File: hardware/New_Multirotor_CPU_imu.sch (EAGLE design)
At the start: 85 parts, among them X2 telemetry, X3 programm, X4 sonar

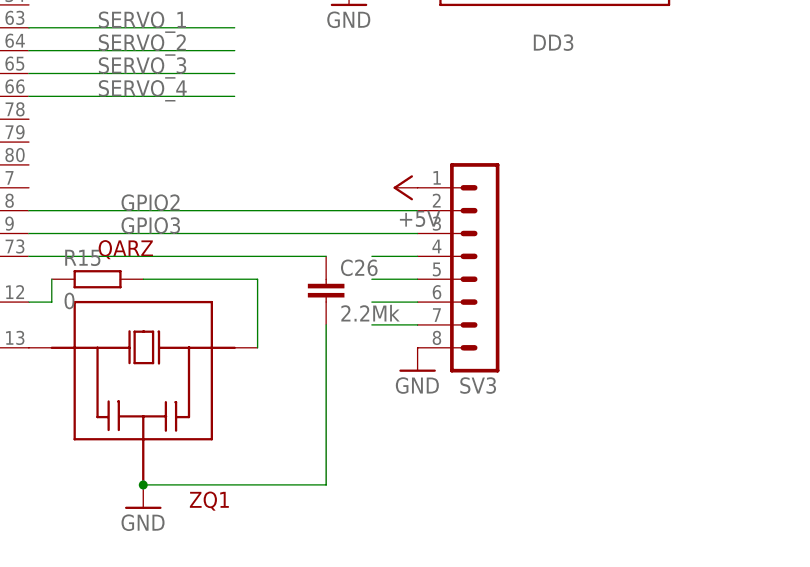
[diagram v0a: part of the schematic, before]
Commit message: Fixes a bug
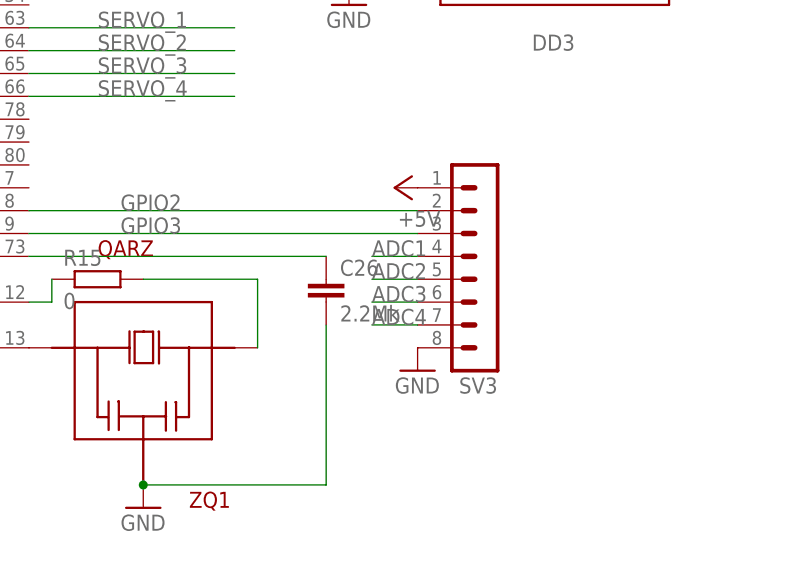
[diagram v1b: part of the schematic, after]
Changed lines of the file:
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@@
 <wire x1="170.18" y1="-12.7" x2="165.1" y2="-12.7" width="0.1524" layer="91"/>
 <pinref part="SV3" gate="1" pin="4"/>
+<label x="165.1" y="-12.7" size="1.778" layer="95"/>
 </segment>
 </net>
@@
 <wire x1="170.18" y1="-20.32" x2="165.1" y2="-20.32" width="0.1524" layer="91"/>
 <pinref part="SV3" gate="1" pin="7"/>
+<label x="165.1" y="-20.32" size="1.778" layer="95"/>
 </segment>
 </net>
@@
 <wire x1="170.18" y1="-15.24" x2="165.1" y2="-15.24" width="0.1524" layer="91"/>
 <pinref part="SV3" gate="1" pin="5"/>
+<label x="165.1" y="-15.24" size="1.778" layer="95"/>
 </segment>
 </net>
@@
 <wire x1="170.18" y1="-17.78" x2="165.1" y2="-17.78" width="0.1524" layer="91"/>
 <pinref part="SV3" gate="1" pin="6"/>
-</segment>
-</net>
+<label x="165.1" y="-17.78" size="1.778" layer="95"/>
+</segment>
+</net>

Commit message: Перезалил
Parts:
- removed R11: 0, resistor:R-EU_R0603
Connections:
- removed net N$15: R11.2, R24.1
- removed net XZ1: DD1.PD12, SV2.8
- removed net XZ2: DD1.PD13, DD6.CS, R10.2, SV2.7
- new net CS_FLASH: DD1.PD13, DD6.CS, R10.2
- net +5V: now also RADIO_IN.8; no longer RADIO_IN.10
- net GND: now also RADIO_IN.10; no longer RADIO_IN.8
- net N$7: now also R24.1; no longer R11.1
- net XZ3: now also SV2.7
- net XZ4: now also SV2.8
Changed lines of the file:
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@@
 <part name="R10" library="resistor" deviceset="R-EU_" device="R0603" value="10k"/>
 <part name="P+22" library="supply1" deviceset="VCC" device=""/>
-<part name="R11" library="resistor" deviceset="R-EU_" device="R0603" value="0"/>
 <part name="R13" library="resistor" deviceset="R-EU_" device="R0603" value="0"/>
 <part name="GND29" library="supply1" deviceset="GND" device=""/>
@@
 <instance part="RN2" gate="C" x="73.66" y="149.86" rot="R180"/>
 <instance part="RN2" gate="D" x="99.06" y="149.86"/>
-<instance part="P+17" gate="1" x="78.74" y="185.42"/>
-<instance part="GND11" gate="1" x="68.58" y="154.94" rot="R270"/>
+<instance part="P+17" gate="1" x="73.66" y="175.26"/>
+<instance part="GND11" gate="1" x="58.42" y="157.48" rot="R270"/>
 <instance part="P+20" gate="VCC" x="220.98" y="25.4" rot="R270"/>
 <instance part="DA2" gate="G$1" x="-139.7" y="-96.52"/>
@@
 <instance part="R10" gate="G$1" x="228.6" y="-27.94" rot="R90"/>
 <instance part="P+22" gate="VCC" x="228.6" y="-35.56" rot="R180"/>
-<instance part="R11" gate="G$1" x="-83.82" y="-88.9"/>
 <instance part="R13" gate="G$1" x="-33.02" y="-93.98"/>
 <instance part="GND29" gate="1" x="-40.64" y="-93.98" rot="R270"/>
@@
 </segment>
 <segment>
-<pinref part="RADIO_IN" gate="G$1" pin="8"/>
-<pinref part="GND11" gate="1" pin="GND"/>
-<wire x1="71.12" y1="154.94" x2="78.74" y2="154.94" width="0.1524" layer="91"/>
-</segment>
-<segment>
 <pinref part="C7" gate="G$1" pin="2"/>
 <pinref part="GND13" gate="1" pin="GND"/>
@@
 <pinref part="GND37" gate="1" pin="GND"/>
 </segment>
+<segment>
+<pinref part="RADIO_IN" gate="G$1" pin="10"/>
+<pinref part="GND11" gate="1" pin="GND"/>
+<wire x1="60.96" y1="157.48" x2="78.74" y2="157.48" width="0.1524" layer="91"/>
+</segment>
 </net>
 <net name="N$41" class="0">
@@
 </segment>
 <segment>
-<pinref part="RADIO_IN" gate="G$1" pin="10"/>
-<pinref part="P+17" gate="1" pin="+5V"/>
-<wire x1="78.74" y1="157.48" x2="78.74" y2="182.88" width="0.1524" layer="91"/>
-</segment>
-<segment>
 <wire x1="236.22" y1="-66.04" x2="228.6" y2="-66.04" width="0.1524" layer="91"/>
 <pinref part="P+7" gate="1" pin="+5V"/>
@@
 <pinref part="SV3" gate="1" pin="1"/>
 <pinref part="P+18" gate="1" pin="+5V"/>
+</segment>
+<segment>
+<pinref part="RADIO_IN" gate="G$1" pin="8"/>
+<wire x1="78.74" y1="154.94" x2="73.66" y2="154.94" width="0.1524" layer="91"/>
+<wire x1="73.66" y1="154.94" x2="73.66" y2="172.72" width="0.1524" layer="91"/>
+<pinref part="P+17" gate="1" pin="+5V"/>
 </segment>
 </net>
@@
 </segment>
 </net>
-<net name="XZ1" class="0">
-<segment>
-<pinref part="DD1" gate="G$1" pin="PD12"/>
-<wire x1="33.02" y1="-15.24" x2="5.08" y2="-15.24" width="0.1524" layer="91"/>
-<label x="5.08" y="-15.24" size="1.778" layer="95"/>
+<net name="CS_FLASH" class="0">
+<segment>
+<pinref part="DD1" gate="G$1" pin="PD13"/>
+<wire x1="33.02" y1="-17.78" x2="5.08" y2="-17.78" width="0.1524" layer="91"/>
+<label x="5.08" y="-17.78" size="1.778" layer="95"/>
+</segment>
+<segment>
+<pinref part="DD6" gate="G$1" pin="CS"/>
+<wire x1="231.14" y1="-22.86" x2="228.6" y2="-22.86" width="0.1524" layer="91"/>
+<label x="220.98" y="-22.86" size="1.778" layer="95"/>
+<pinref part="R10" gate="G$1" pin="2"/>
+<junction x="228.6" y="-22.86"/>
+<wire x1="228.6" y1="-22.86" x2="220.98" y2="-22.86" width="0.1524" layer="91"/>
+</segment>
+</net>
+<net name="XZ3" class="0">
+<segment>
+<pinref part="DD1" gate="G$1" pin="PD14"/>
+<wire x1="33.02" y1="-20.32" x2="5.08" y2="-20.32" width="0.1524" layer="91"/>
+<label x="5.08" y="-20.32" size="1.778" layer="95"/>
+</segment>
+<segment>
+<pinref part="SV2" gate="G$1" pin="7"/>
+<wire x1="251.46" y1="-63.5" x2="261.62" y2="-63.5" width="0.1524" layer="91"/>
+<label x="256.54" y="-63.5" size="1.778" layer="95"/>
+</segment>
+</net>
+<net name="XZ4" class="0">
+<segment>
+<pinref part="DD1" gate="G$1" pin="PD15"/>
+<wire x1="33.02" y1="-22.86" x2="5.08" y2="-22.86" width="0.1524" layer="91"/>
+<label x="5.08" y="-22.86" size="1.778" layer="95"/>
 </segment>
 <segment>
@@
 <wire x1="236.22" y1="-63.5" x2="228.6" y2="-63.5" width="0.1524" layer="91"/>
 <label x="231.14" y="-63.5" size="1.778" layer="95"/>
-</segment>
-</net>
-<net name="XZ2" class="0">
-<segment>
-<pinref part="DD1" gate="G$1" pin="PD13"/>
-<wire x1="33.02" y1="-17.78" x2="5.08" y2="-17.78" width="0.1524" layer="91"/>
-<label x="5.08" y="-17.78" size="1.778" layer="95"/>
-</segment>
-<segment>
-<pinref part="SV2" gate="G$1" pin="7"/>
-<wire x1="251.46" y1="-63.5" x2="261.62" y2="-63.5" width="0.1524" layer="91"/>
-<label x="256.54" y="-63.5" size="1.778" layer="95"/>
-</segment>
-<segment>
-<pinref part="DD6" gate="G$1" pin="CS"/>
-<wire x1="231.14" y1="-22.86" x2="228.6" y2="-22.86" width="0.1524" layer="91"/>
-<label x="223.52" y="-22.86" size="1.778" layer="95"/>
-<pinref part="R10" gate="G$1" pin="2"/>
-<junction x="228.6" y="-22.86"/>
-<wire x1="228.6" y1="-22.86" x2="220.98" y2="-22.86" width="0.1524" layer="91"/>
-</segment>
-</net>
-<net name="XZ3" class="0">
-<segment>
-<pinref part="DD1" gate="G$1" pin="PD14"/>
-<wire x1="33.02" y1="-20.32" x2="5.08" y2="-20.32" width="0.1524" layer="91"/>
-<label x="5.08" y="-20.32" size="1.778" layer="95"/>
-</segment>
-</net>
-<net name="XZ4" class="0">
-<segment>
-<pinref part="DD1" gate="G$1" pin="PD15"/>
-<wire x1="33.02" y1="-22.86" x2="5.08" y2="-22.86" width="0.1524" layer="91"/>
-<label x="5.08" y="-22.86" size="1.778" layer="95"/>
 </segment>
 </net>
@@
 <wire x1="-99.06" y1="-88.9" x2="-88.9" y2="-88.9" width="0.1524" layer="91"/>
 <pinref part="R6" gate="G$1" pin="1"/>
-<pinref part="R11" gate="G$1" pin="1"/>
+<pinref part="R24" gate="G$1" pin="1"/>
+<wire x1="-88.9" y1="-88.9" x2="-78.74" y2="-88.9" width="0.1524" layer="91"/>
 <junction x="-88.9" y="-88.9"/>
 </segment>
 </net>
-<net name="N$15" class="0">
-<segment>
-<pinref part="R11" gate="G$1" pin="2"/>
-<pinref part="R24" gate="G$1" pin="1"/>
-</segment>
-</net>
